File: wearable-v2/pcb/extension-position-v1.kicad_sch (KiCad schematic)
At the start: 19 parts, among them IC1 TESEO-LIV3F, J5 EXT_3_SOCKET, U14 LIS2DE12

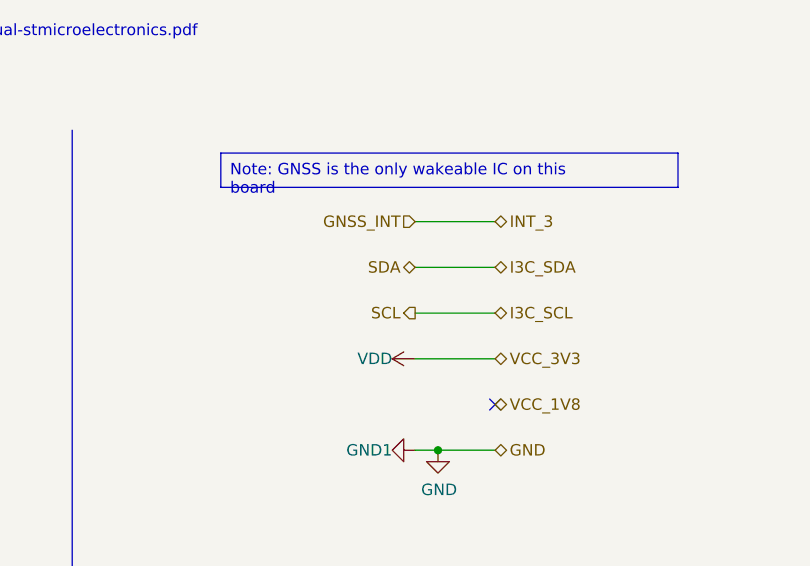
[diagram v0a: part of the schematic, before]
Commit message: Updated components and PCB layout
Signed-off-by: Adam Fowler <adam@adamfowler.org>
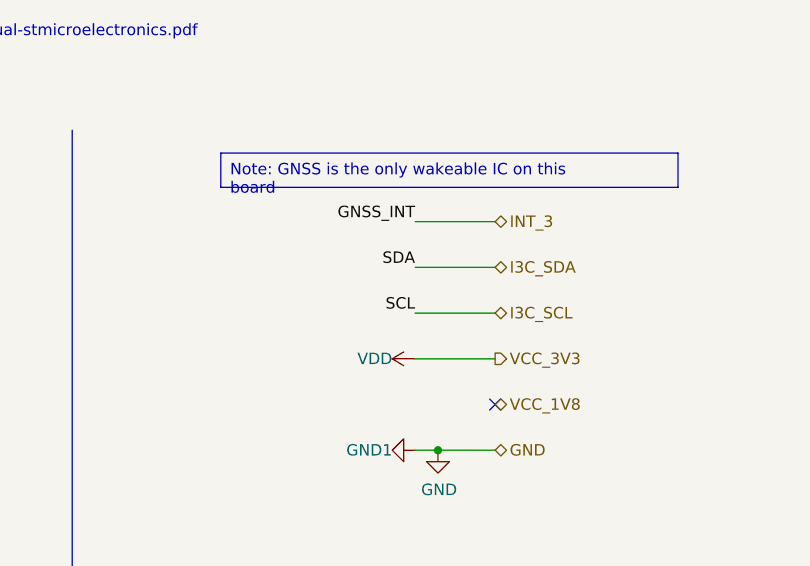
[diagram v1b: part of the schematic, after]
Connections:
- net GNSS_INT renamed INT_3
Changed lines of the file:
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@@
+    (effects (font (size 1.27 1.27)) (justify right bottom))
+  )
+  (label "SDA" (at 172.72 43.18 180) (fields_autoplaced)
     (effects (font (size 1.27 1.27)) (justify right bottom))
   )
   (label "ACC_INT2" (at 189.23 129.54 0) (fields_autoplaced)
     (effects (font (size 1.27 1.27)) (justify left bottom))
+  )
+  (label "GNSS_INT" (at 172.72 38.1 180) (fields_autoplaced)
+    (effects (font (size 1.27 1.27)) (justify right bottom))
   )
   (label "SDA" (at 166.37 127 180) (fields_autoplaced)
@@
     (effects (font (size 1.27 1.27)) (justify left bottom))
   )
+  (label "SCL" (at 172.72 48.26 180) (fields_autoplaced)
+    (effects (font (size 1.27 1.27)) (justify right bottom))
+  )
   (label "GNSS_INT" (at 46.99 52.07 180) (fields_autoplaced)
     (effects (font (size 1.27 1.27)) (justify right bottom))
@@
   (hierarchical_label "I3C_SDA" (shape bidirectional) (at 256.54 43.18 0) (fields_autoplaced)
     (effects (font (size 1.27 1.27)) (justify left))
-  )
-  (hierarchical_label "SCL" (shape output) (at 172.72 48.26 180) (fields_autoplaced)
-    (effects (font (size 1.27 1.27)) (justify right))
   )
   (hierarchical_label "VCC_1V8" (shape bidirectional) (at 256.54 58.42 0) (fields_autoplaced)
@@
     (effects (font (size 1.27 1.27)) (justify left))
   )
-  (hierarchical_label "SDA" (shape bidirectional) (at 172.72 43.18 180) (fields_autoplaced)
-    (effects (font (size 1.27 1.27)) (justify right))
-  )
-  (hierarchical_label "GNSS_INT" (shape input) (at 172.72 38.1 180) (fields_autoplaced)
-    (effects (font (size 1.27 1.27)) (justify right))
-  )
-  (hierarchical_label "VCC_3V3" (shape bidirectional) (at 181.61 53.34 0) (fields_autoplaced)
+  (hierarchical_label "VCC_3V3" (shape output) (at 181.61 53.34 0) (fields_autoplaced)
     (effects (font (size 1.27 1.27)) (justify left))
   )

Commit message: Further V2 routing
Signed-off-by: Adam Fowler <adam@adamfowler.org>
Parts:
- ANT1: footprint Herald_Extras:NN02-224 -> Herald:NN02-224
- IC1: footprint Herald_Extras:SON110P970X1010X230-18N -> Herald:SON110P970X1010X230-18N
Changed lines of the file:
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@@
       (effects (font (size 1.27 1.27)))
     )
-    (property "Footprint" "Herald_Extras:NN02-224" (at 252.73 128.27 0)
+    (property "Footprint" "Herald:NN02-224" (at 252.73 128.27 0)
       (effects (font (size 1.27 1.27)) hide)
     )
@@
       (effects (font (size 1.27 1.27)))
     )
-    (property "Footprint" "Herald_Extras:SON110P970X1010X230-18N" (at 71.12 39.37 0)
+    (property "Footprint" "Herald:SON110P970X1010X230-18N" (at 71.12 39.37 0)
       (effects (font (size 1.27 1.27)) (justify bottom) hide)
     )

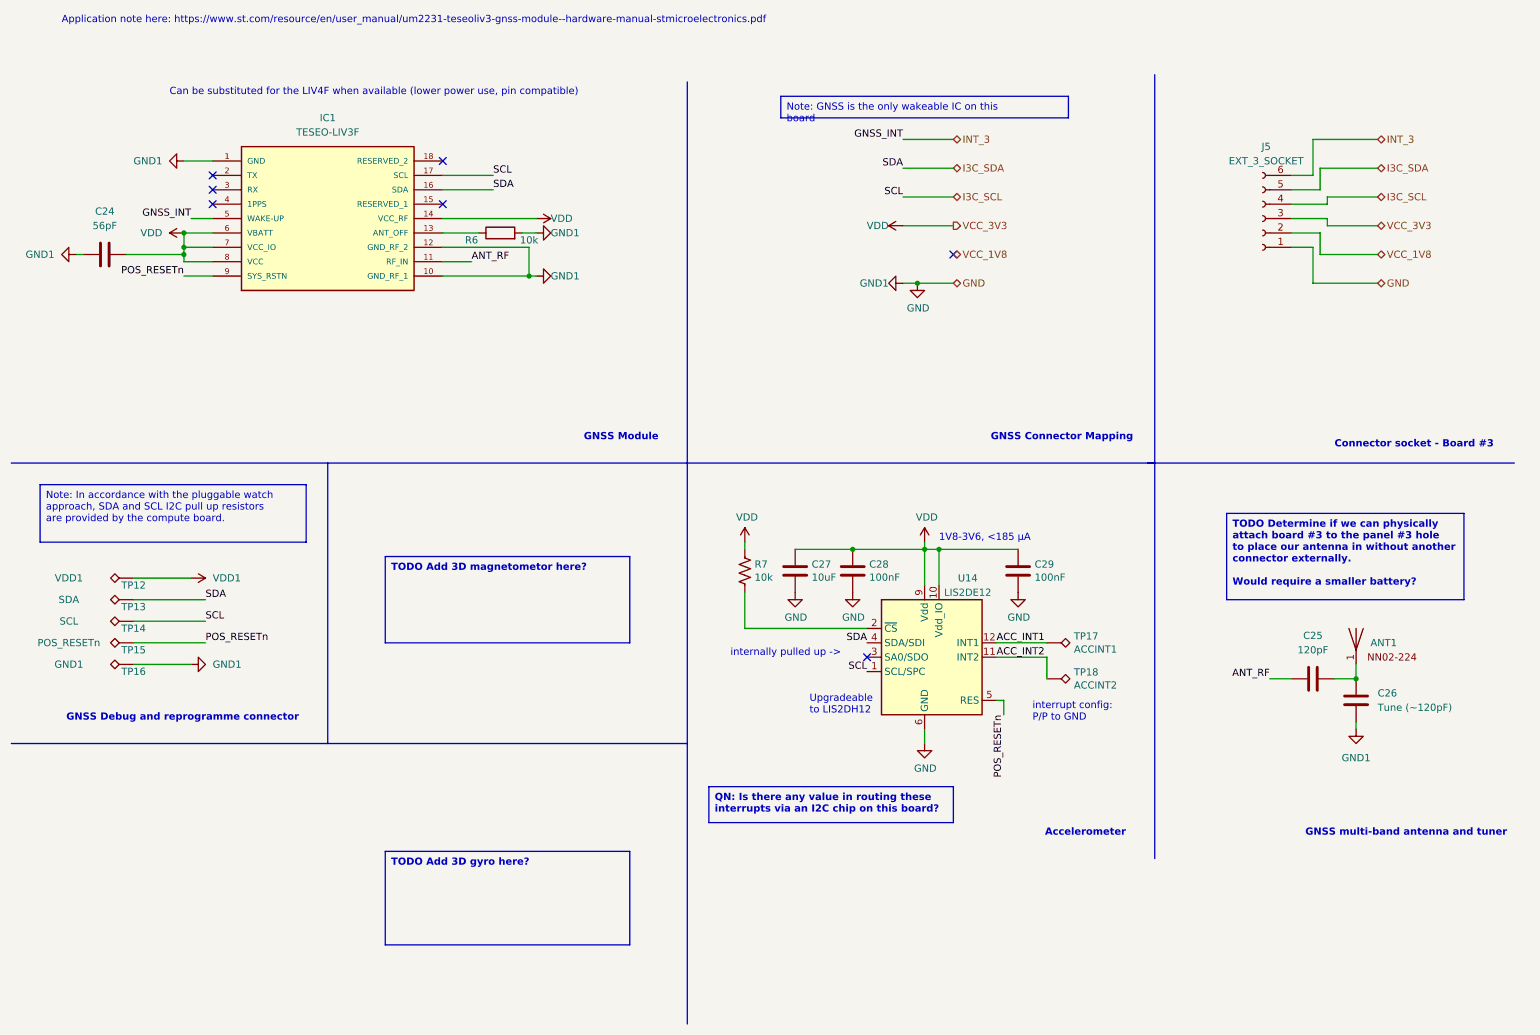
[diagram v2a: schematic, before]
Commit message: Added front connectors on main board
Signed-off-by: Adam Fowler <adam@adamfowler.org>
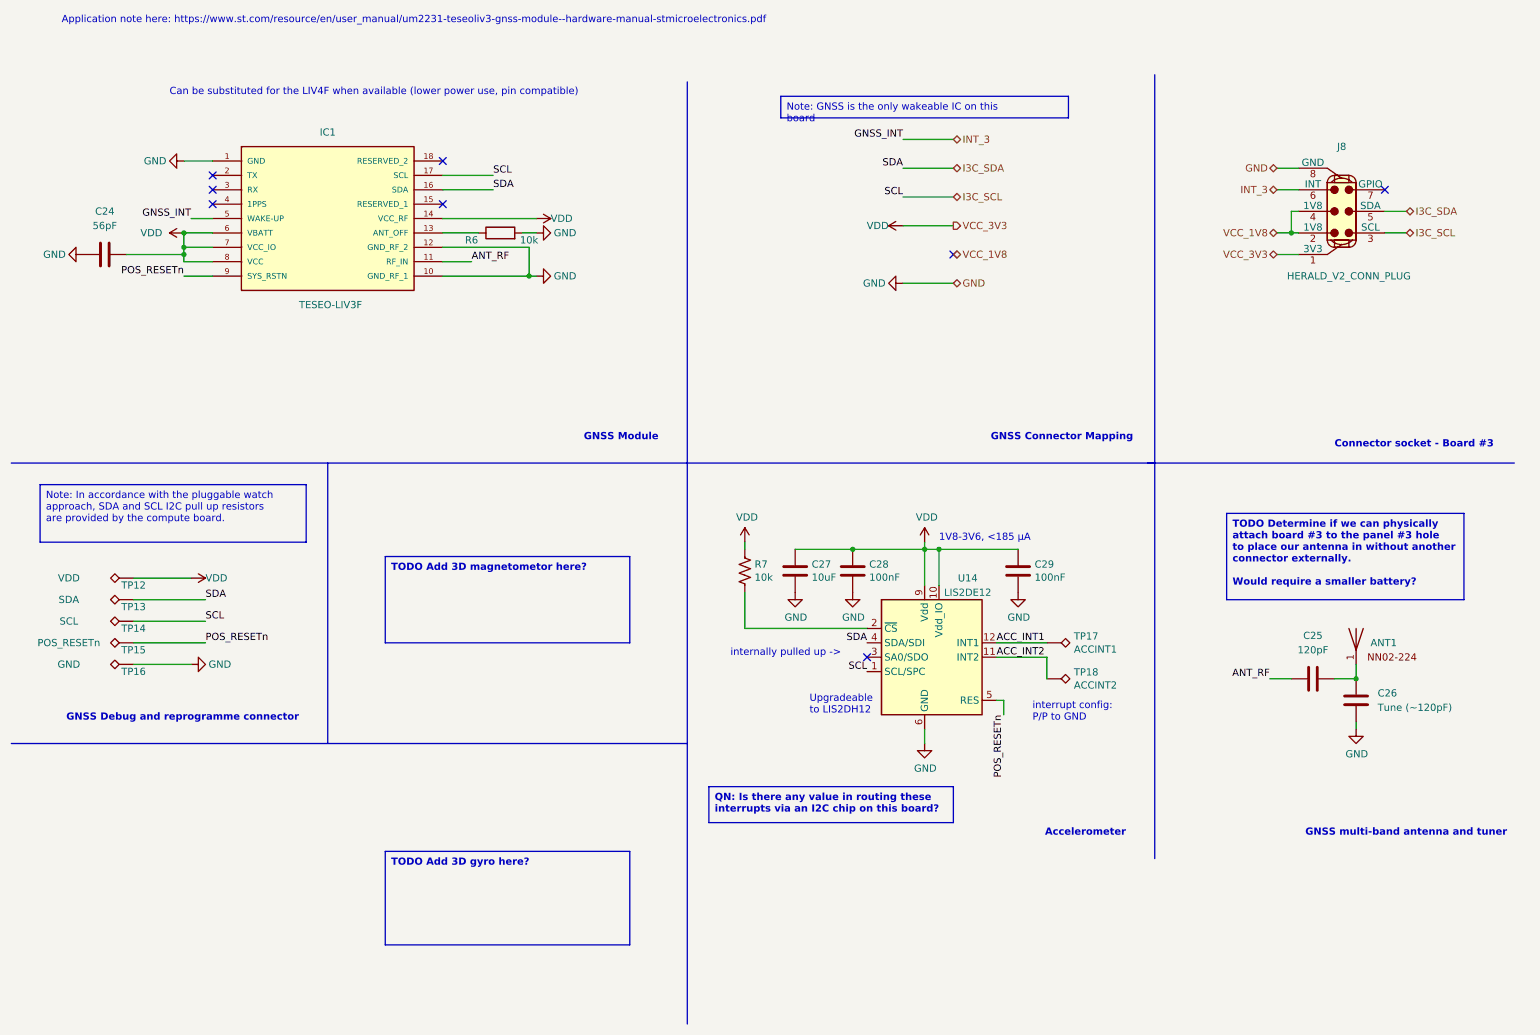
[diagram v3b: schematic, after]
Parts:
- removed J5: EXT_3_SOCKET, symbol Connector:Conn_01x06_Socket
- added J8: HERALD_V2_CONN_PLUG, symbol Herald_Extras:HERALD_V2_CONN_PLUG
- IC1: footprint Herald:SON110P970X1010X230-18N -> SON110P970X1010X230-18N
- TP12: value VDD1 -> VDD
- TP16: value GND1 -> GND
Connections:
- net GND: now also J8.8 (GND)
- net I3C_SCL: now also J8.3 (SCL)
- net I3C_SDA: now also J8.5 (SDA)
- net INT_3: now also J8.6 (INT)
- net VCC_1V8: now also J8.2 (1V8), J8.4 (1V8)
- net VDD1: now also J8.1 (3V3)
- no-connect marks 7 -> 8

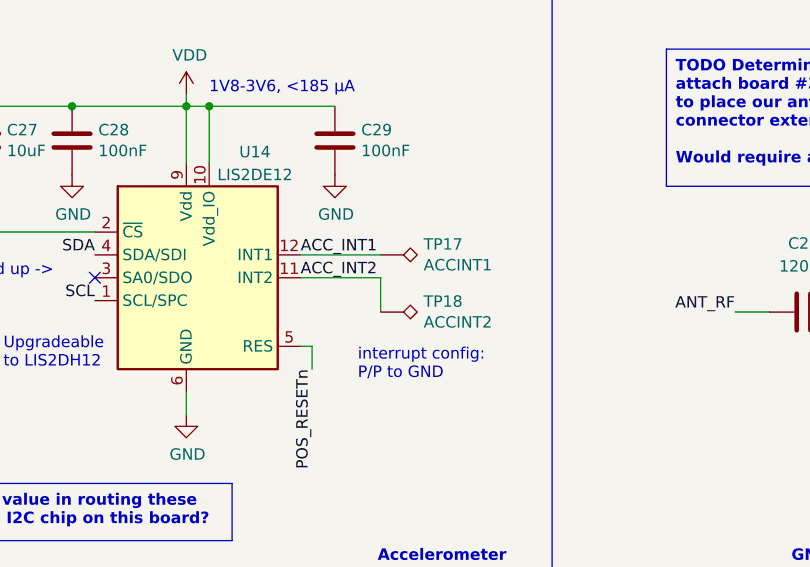
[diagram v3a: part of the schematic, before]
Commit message: Set wider PCB GND tracks and vias
Signed-off-by: Adam Fowler <adam@adamfowler.org>
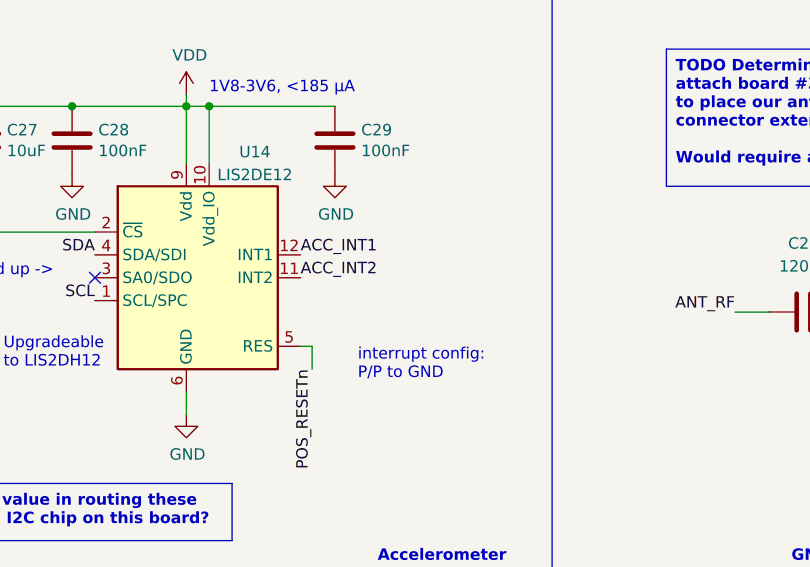
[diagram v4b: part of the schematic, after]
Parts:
- removed TP17: ACCINT1, TestPoint:TestPoint_Pad_D1.0mm, symbol Connector:TestPoint_Alt
- removed TP18: ACCINT2, TestPoint:TestPoint_Pad_D1.0mm, symbol Connector:TestPoint_Alt
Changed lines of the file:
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@@
-    (stroke (width 0) (type default))
-  )
-  (wire (pts (xy 198.12 133.35) (xy 198.12 129.54))
     (stroke (width 0) (type default))
   )
@@
     (stroke (width 0) (type default))
   )
-  (wire (pts (xy 198.12 127) (xy 189.23 127))
-    (stroke (width 0) (type default))
-  )
   (wire (pts (xy 91.44 44.45) (xy 100.33 44.45))
     (stroke (width 0) (type default))
@@
   )
   (wire (pts (xy 45.72 54.61) (xy 45.72 57.15))
-    (stroke (width 0) (type default))
-  )
-  (wire (pts (xy 198.12 129.54) (xy 189.23 129.54))
     (stroke (width 0) (type default))
   )
@@
         (path "/bdd943b2-035a-4beb-80ad-5c7e84260dde/00000000-0000-0000-0000-000060f1d377"
           (reference "R41") (unit 1)
-        )
-      )
-    )
-  )
-  (symbol (lib_id "Connector:TestPoint_Alt") (at 198.12 133.35 270) (unit 1)
-    (in_bom yes) (on_board yes) (dnp no)
-    (property "Reference" "TP18" (at 202.8952 132.1816 90)
-      (effects (font (size 1.27 1.27)) (justify left))
-    )
-    (property "Value" "ACCINT2" (at 202.8952 134.493 90)
-      (effects (font (size 1.27 1.27)) (justify left))
-    )
-    (property "Footprint" "TestPoint:TestPoint_Pad_D1.0mm" (at 198.12 138.43 0)
-      (effects (font (size 1.27 1.27)) hide)
-    )
-    (property "Datasheet" "~" (at 198.12 138.43 0)
-      (effects (font (size 1.27 1.27)) hide)
-    )
-    (property "Description" "Test point" (at 198.12 133.35 0)
-      (effects (font (size 1.27 1.27)) hide)
-    )
-    (property "MPN" "~" (at 198.12 133.35 0)
-      (effects (font (size 1.27 1.27)) hide)
-    )
-    (pin "1")
-    (instances
-      (project "wearable-v2"
-        (path "/1eb7e8c9-86dc-4f6b-85aa-748b782af952/310cdce3-d5fc-4499-9461-bc61ed18b264"
-          (reference "TP18") (unit 1)
-        )
-      )
-      (project "wearable"
-        (path "/bdd943b2-035a-4beb-80ad-5c7e84260dde/00000000-0000-0000-0000-000060f1d377"
-          (reference "TP42") (unit 1)
         )
       )
@@
         )
       )
-    )
-  )
-  (symbol (lib_id "Connector:TestPoint_Alt") (at 198.12 127 270) (unit 1)
-    (in_bom yes) (on_board yes) (dnp no)
-    (property "Reference" "TP17" (at 202.8952 125.8316 90)
-      (effects (font (size 1.27 1.27)) (justify left))
-    )
-    (property "Value" "ACCINT1" (at 202.8952 128.143 90)
-      (effects (font (size 1.27 1.27)) (justify left))
-    )
-    (property "Footprint" "TestPoint:TestPoint_Pad_D1.0mm" (at 198.12 132.08 0)
-      (effects (font (size 1.27 1.27)) hide)
-    )
-    (property "Datasheet" "~" (at 198.12 132.08 0)
-      (effects (font (size 1.27 1.27)) hide)
-    )
-    (property "Description" "Test point" (at 198.12 127 0)
-      (effects (font (size 1.27 1.27)) hide)
-    )
-    (property "MPN" "~" (at 198.12 127 0)
-      (effects (font (size 1.27 1.27)) hide)
-    )
-    (pin "1")
-    (instances
-      (project "wearable-v2"
-        (path "/1eb7e8c9-86dc-4f6b-85aa-748b782af952/310cdce3-d5fc-4499-9461-bc61ed18b264"
-          (reference "TP17") (unit 1)
-        )
-      )
-      (project "wearable"
-        (path "/bdd943b2-035a-4beb-80ad-5c7e84260dde/00000000-0000-0000-0000-000060f1d377"
-          (reference "TP41") (unit 1)
-        )
-      )

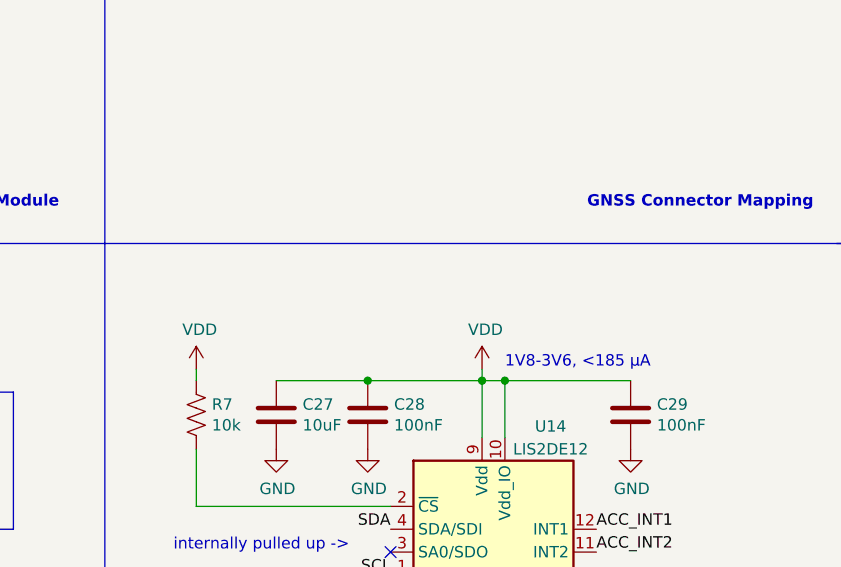
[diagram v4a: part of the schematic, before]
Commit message: Added I2C and I3C notes and additional resistors
Signed-off-by: Adam Fowler <adam@adamfowler.org>
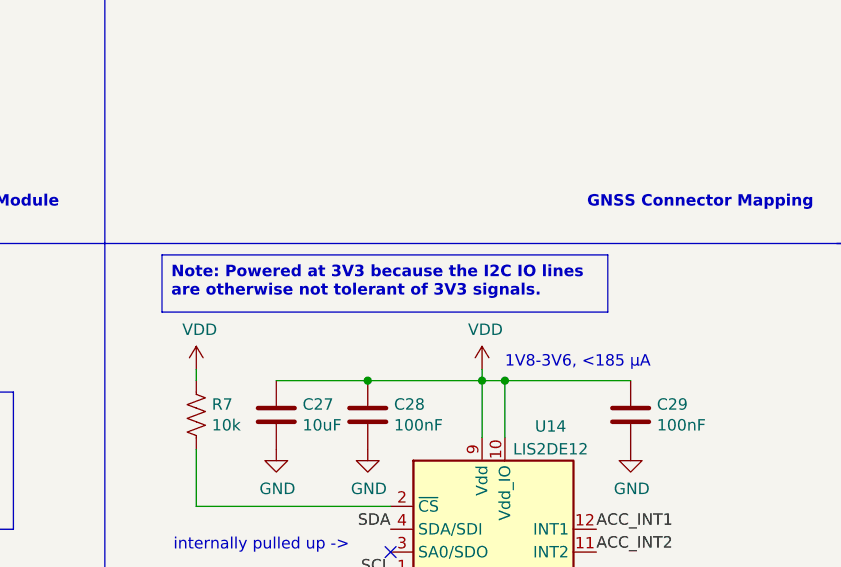
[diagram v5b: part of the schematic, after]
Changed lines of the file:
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@@
     (effects (font (size 1.27 1.27)) (justify left top))
+  )
+  (text_box "Note: Powered at 3V3 because the I2C IO lines are otherwise not tolerant of 3V3 signals."
+    (at 140.97 96.52 0) (size 49.53 6.35)
+    (stroke (width 0) (type default))
+    (fill (type none))
+    (effects (font (size 1.27 1.27) bold) (justify left top))
   )
   (text_box "QN: Is there any value in routing these interrupts via an I2C chip on this board?"
